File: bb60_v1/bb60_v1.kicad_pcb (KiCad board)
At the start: 2 copper layers, 145 parts, among them J1 Conn_01x04, SW1 SW_Push, SW2 SW_Push, U1 STM32F072CBTx, U2 XC6206PxxxMR, U3 USBLC6-2SC6

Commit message: rearranging pcb
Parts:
- moved C7 63.1 mm to (126.5, 175.0)
- moved C1 60.6 mm to (126.5, 171.5)
- moved C8 60.1 mm to (123.6, 175.0)
- moved C2 58.2 mm to (124.1, 171.5)
- moved C9 57.2 mm to (120.6, 175.0)
- moved C3 55.6 mm to (121.4, 171.5)
- moved C5 53.6 mm to (117.0, 171.5)
- moved C4 53.4 mm to (119.1, 171.5)
- moved C6 32.6 mm to (97.3, 172.6)
- moved R1 30.5 mm to (91.4, 172.0)
- moved R2 27.5 mm to (88.5, 172.0)
- moved R3 24.6 mm to (85.5, 172.0)
- moved U1 0.40 mm to (109.6, 174.4)
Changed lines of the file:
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@@
 	(footprint "Capacitor_SMD:C_0201_0603Metric"
 		(layer "B.Cu")
-		(at 63.448125 176.140625 180)
+		(at 120.598226 175.022022 180)
 		(descr "Capacitor SMD 0201 (0603 Metric), square (rectangular) end terminal, IPC-7351 nominal, (Body size source: https://www.vishay.com/docs/20052/crcw0201e3.pdf)")
 		(tags "capacitor")
@@
 	(footprint "Capacitor_SMD:C_0201_0603Metric"
 		(layer "B.Cu")
-		(at 65.898125 170.890625 180)
+		(at 126.456669 171.450144 180)
 		(descr "Capacitor SMD 0201 (0603 Metric), square (rectangular) end terminal, IPC-7351 nominal, (Body size source: https://www.vishay.com/docs/20052/crcw0201e3.pdf)")
 		(tags "capacitor")
@@
 	(footprint "Capacitor_SMD:C_0201_0603Metric"
 		(layer "B.Cu")
-		(at 63.448125 172.640625 180)
+		(at 126.456669 175.022022 180)
 		(descr "Capacitor SMD 0201 (0603 Metric), square (rectangular) end terminal, IPC-7351 nominal, (Body size source: https://www.vishay.com/docs/20052/crcw0201e3.pdf)")
 		(tags "capacitor")
@@
 	(footprint "Resistor_SMD:R_0201_0603Metric"
 		(layer "B.Cu")
-		(at 60.998125 170.890625 180)
+		(at 91.427889 172.045457 180)
 		(descr "Resistor SMD 0201 (0603 Metric), square (rectangular) end terminal, IPC-7351 nominal, (Body size source: https://www.vishay.com/docs/20052/crcw0201e3.pdf)")
 		(tags "resistor")
@@
 	(footprint "Capacitor_SMD:C_0201_0603Metric"
 		(layer "B.Cu")
-		(at 63.448125 170.890625 180)
+		(at 117.026348 171.450144 180)
 		(descr "Capacitor SMD 0201 (0603 Metric), square (rectangular) end terminal, IPC-7351 nominal, (Body size source: https://www.vishay.com/docs/20052/crcw0201e3.pdf)")
 		(tags "capacitor")
@@
 	(footprint "Resistor_SMD:R_0201_0603Metric"
 		(layer "B.Cu")
-		(at 60.998125 174.390625 180)
+		(at 85.474759 172.045457 180)
 		(descr "Resistor SMD 0201 (0603 Metric), square (rectangular) end terminal, IPC-7351 nominal, (Body size source: https://www.vishay.com/docs/20052/crcw0201e3.pdf)")
 		(tags "resistor")
@@
 	(footprint "Resistor_SMD:R_0201_0603Metric"
 		(layer "B.Cu")
-		(at 60.998125 172.640625 180)
+		(at 88.451324 172.045457 180)
 		(descr "Resistor SMD 0201 (0603 Metric), square (rectangular) end terminal, IPC-7351 nominal, (Body size source: https://www.vishay.com/docs/20052/crcw0201e3.pdf)")
 		(tags "resistor")
@@
 	(footprint "Package_QFP:LQFP-48_7x7mm_P0.5mm"
 		(layer "B.Cu")
-		(at 109.35875 174.11375 180)
+		(at 109.63766 174.400123 180)
 		(descr "LQFP, 48 Pin (JEDEC MS-026 variation BBC, 1.40mm body thickness, https://www.jedec.org/document_search?search_api_views_fulltext=MS-026, https://www.analog.com/media/en/package-pcb-resources/package/pkg_pdf/ltc-legacy-lqfp/05081760_a_lx48.pdf)")
 		(tags "LQFP QFP CASE-932AA CASE-932-03 C48-1 C48-2 C48-3 C48-5 C48-6 C48-6C PT0048A")
@@
 	(footprint "Capacitor_SMD:C_0201_0603Metric"
 		(layer "B.Cu")
-		(at 65.898125 172.640625 180)
+		(at 124.075417 171.450144 180)
 		(descr "Capacitor SMD 0201 (0603 Metric), square (rectangular) end terminal, IPC-7351 nominal, (Body size source: https://www.vishay.com/docs/20052/crcw0201e3.pdf)")
 		(tags "capacitor")
@@
 		)
 		(property "Value" "1N4148"
-			(at -35.82 -20.75 90)
+			(at -0.317673 -2.14298 90)
 			(layer "B.Fab")
 			(effects
@@
 	(footprint "Capacitor_SMD:C_0805_2012Metric"
 		(layer "B.Cu")
-		(at 65.481875 165.655625 180)
+		(at 97.276645 172.64077 180)
 		(descr "Capacitor SMD 0805 (2012 Metric), square (rectangular) end terminal, IPC-7351 nominal, (Body size source: IPC-SM-782 page 76, https://www.pcb-3d.com/wordpress/wp-content/uploads/ipc-sm-782a_amendment_1_and_2.pdf, https://docs.google.com/spreadsheets/d/1BsfQQcO9C6DZCsRaXUlFlo91Tg2WpOkGARC1WS5S8t0/edit?usp=sharing)")
 		(tags "capacitor")
@@
 	(footprint "Capacitor_SMD:C_0201_0603Metric"
 		(layer "B.Cu")
-		(at 65.898125 174.390625 180)
+		(at 121.443852 171.450144 180)
 		(descr "Capacitor SMD 0201 (0603 Metric), square (rectangular) end terminal, IPC-7351 nominal, (Body size source: https://www.vishay.com/docs/20052/crcw0201e3.pdf)")
 		(tags "capacitor")
@@
 	(footprint "Capacitor_SMD:C_0201_0603Metric"
 		(layer "B.Cu")
-		(at 65.898125 176.140625 180)
+		(at 119.0626 171.450144 180)
 		(descr "Capacitor SMD 0201 (0603 Metric), square (rectangular) end terminal, IPC-7351 nominal, (Body size source: https://www.vishay.com/docs/20052/crcw0201e3.pdf)")
 		(tags "capacitor")
@@
 	(footprint "Capacitor_SMD:C_0201_0603Metric"
 		(layer "B.Cu")
-		(at 63.448125 174.390625 180)
+		(at 123.574791 175.022022 180)
 		(descr "Capacitor SMD 0201 (0603 Metric), square (rectangular) end terminal, IPC-7351 nominal, (Body size source: https://www.vishay.com/docs/20052/crcw0201e3.pdf)")
 		(tags "capacitor")

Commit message: new traces made
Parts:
- moved D54 1.55 mm to (332.8, 205.7)
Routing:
- net /COL0: track 45.8 -> 115.0 mm, vias 0 -> 1
- net /COL12: track 62.3 -> 109.3 mm
- net /COL2: track 91.7 -> 125.7 mm, vias 0 -> 2
- net /COL1: track 85.1 -> 96.9 mm
- net Net-(D43-A): track 0.00 -> 7.17 mm
- net Net-(D41-A): track 0.00 -> 7.17 mm
- net Net-(D54-A): track 0.00 -> 7.12 mm

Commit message: minor changes
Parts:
- moved C1 66.0 mm to (60.6, 166.8)
- moved C2 66.0 mm to (58.2, 166.8)
- moved C3 66.0 mm to (55.6, 166.8)
- moved C4 66.0 mm to (53.2, 166.8)
- moved C5 66.0 mm to (51.2, 166.8)
- moved C6 66.0 mm to (31.4, 168.0)
- moved C7 66.0 mm to (60.6, 170.4)
- moved C8 66.0 mm to (57.7, 170.4)
- moved R2 66.0 mm to (22.6, 167.4)
- moved R3 66.0 mm to (19.6, 167.4)
- moved C9 66.0 mm to (54.8, 170.4)
- moved R1 66.0 mm to (25.6, 167.4)
- moved SW1 66.0 mm to (73.2, 170.1)
- moved SW2 66.0 mm to (67.3, 170.1)
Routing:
- net /ROW0: track 338.7 -> 257.2 mm
- net /ROW4: track 338.2 -> 260.6 mm
- net /ROW3: track 317.4 -> 254.6 mm
- net /ROW2: track 257.8 -> 221.5 mm, vias 2 -> 0
- net /COL2: track 125.7 -> 90.7 mm, vias 2 -> 0
- net /ROW1: track 261.8 -> 233.4 mm, vias 2 -> 0
- net /COL0: track 115.0 -> 91.5 mm, vias 1 -> 0
- net /COL1: track 96.9 -> 84.8 mm
- net /COL12: track 109.3 -> 106.0 mm
- net /COL6: track 95.1 -> 92.7 mm
- net /COL4: track 68.7 -> 67.7 mm
- net /COL11: track 88.0 -> 87.4 mm
- net /COL8: track 68.2 -> 67.7 mm

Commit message: added pcb outline to pcb
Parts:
- moved C6 127.3 mm to (43.3, 41.3)
- moved R1 127.3 mm to (37.4, 40.7)
- moved R2 127.3 mm to (34.4, 40.7)
- moved R3 127.3 mm to (31.5, 40.7)
- moved SW1 127.3 mm to (85.0, 43.3)
- moved SW2 127.3 mm to (79.1, 43.3)
- moved C1 127.3 mm to (72.4, 40.1)
- moved C2 127.3 mm to (70.1, 40.1)
- moved C3 127.3 mm to (67.4, 40.1)
- moved C4 127.3 mm to (65.0, 40.1)
- moved C5 127.3 mm to (63.0, 40.1)
- moved C7 127.3 mm to (72.4, 43.6)
- moved C8 127.3 mm to (69.6, 43.6)
- moved C9 127.3 mm to (66.6, 43.6)
- moved U2 67.5 mm to (100.0, 94.5)
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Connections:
- U1 pad 10: /COL6 -> /COL3
- U1 pad 11: /COL5 -> /COL2
- U1 pad 12: /COL4 -> /COL1
- U1 pad 13: /COL3 -> /COL6
- U1 pad 14: /COL2 -> /COL5
- U1 pad 16: /ROW2 -> /ROW4
- U1 pad 18: /ROW4 -> /ROW2
- U1 pad 43: /COL1 -> /COL4
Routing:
- net /COL3: track 67.7 -> 114.5 mm
- net /ROW1: track 233.4 -> 264.1 mm, vias 0 -> 2
- net GND: track 0.00 -> 30.4 mm
- net /COL2: track 90.7 -> 118.1 mm
- net /ROW2: track 221.5 -> 248.1 mm, vias 0 -> 2
- net +5V: track 0.00 -> 24.8 mm
- net /COL0: track 91.5 -> 108.0 mm, vias 0 -> 2
- net +3.3V: track 0.00 -> 10.3 mm, vias 0 -> 2
- net /COL1: track 84.8 -> 92.4 mm
- net /USB_D+: track 0.00 -> 5.38 mm
- net /USB_D-: track 0.00 -> 5.38 mm
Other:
- board outline added: 281 x 94.4 mm

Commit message: Routed traces columns 7-11
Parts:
- moved C1 111.0 mm to (182.7, 52.0)
- moved C4 111.0 mm to (175.3, 52.0)
- moved C7 111.0 mm to (182.7, 55.5)
- moved C8 111.0 mm to (179.9, 55.5)
- moved R3 111.0 mm to (141.8, 52.6)
- moved C2 111.0 mm to (180.4, 52.0)
- moved C3 111.0 mm to (177.7, 52.0)
- moved C5 111.0 mm to (173.3, 52.0)
- moved C6 111.0 mm to (153.6, 53.2)
- moved R1 111.0 mm to (147.7, 52.6)
- moved R2 111.0 mm to (144.7, 52.6)
- moved SW1 111.0 mm to (195.4, 55.2)
- moved SW2 111.0 mm to (189.4, 55.2)
- moved C9 111.0 mm to (176.9, 55.5)
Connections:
- U1 pad 2: /COL11 -> /COL7
- U1 pad 3: /COL10 -> /COL8
- U1 pad 5: /COL8 -> /COL10
- U1 pad 6: /COL7 -> /COL11
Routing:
- net /COL11: track 87.4 -> 281.9 mm, vias 0 -> 1
- net /COL10: track 67.7 -> 242.9 mm, vias 0 -> 1
- net /COL9: track 67.7 -> 223.7 mm, vias 0 -> 1
- net /COL8: track 67.7 -> 204.4 mm, vias 0 -> 1
- net /COL7: track 67.7 -> 185.1 mm, vias 0 -> 1
- net /ROW4: track 260.6 -> 316.7 mm, vias 0 -> 2
- net /ROW3: track 254.6 -> 283.5 mm
- net /ROW2: track 248.1 -> 260.9 mm

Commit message: minor changes
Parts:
- SW1, SW2: moved to F.Cu
- moved C1 128.3 mm to (63.7, 99.9)
- moved C4 128.3 mm to (56.3, 99.9)
- moved C7 128.3 mm to (63.7, 103.4)
- moved C8 128.3 mm to (60.8, 103.4)
- moved R3 128.3 mm to (22.7, 100.4)
- moved C2 128.3 mm to (61.3, 99.9)
- moved C3 128.3 mm to (58.7, 99.9)
- moved C5 128.3 mm to (54.3, 99.9)
- moved C6 128.3 mm to (34.5, 101.0)
- moved C9 128.3 mm to (57.8, 103.4)
- moved R1 128.3 mm to (28.7, 100.4)
- moved R2 128.3 mm to (25.7, 100.4)
- moved SW2 111.5 mm to (242.2, 153.5)
- moved SW1 105.1 mm to (232.7, 153.5)

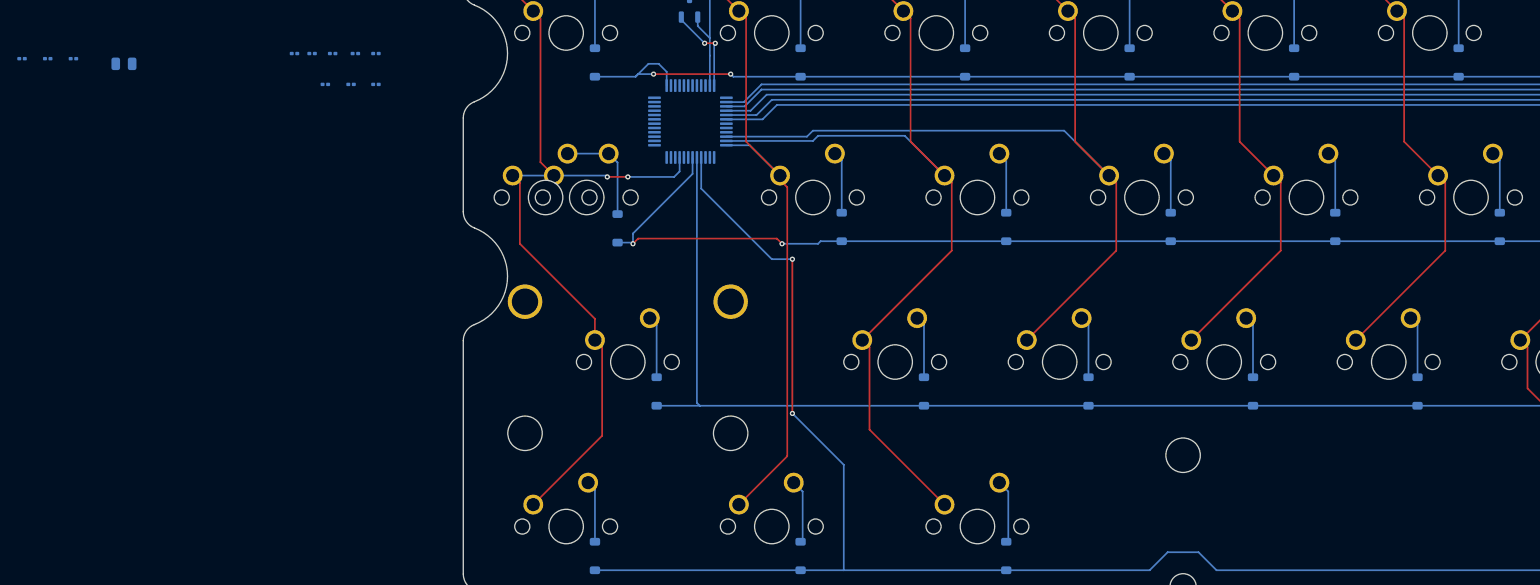
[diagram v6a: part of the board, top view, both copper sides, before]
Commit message: test export fab files
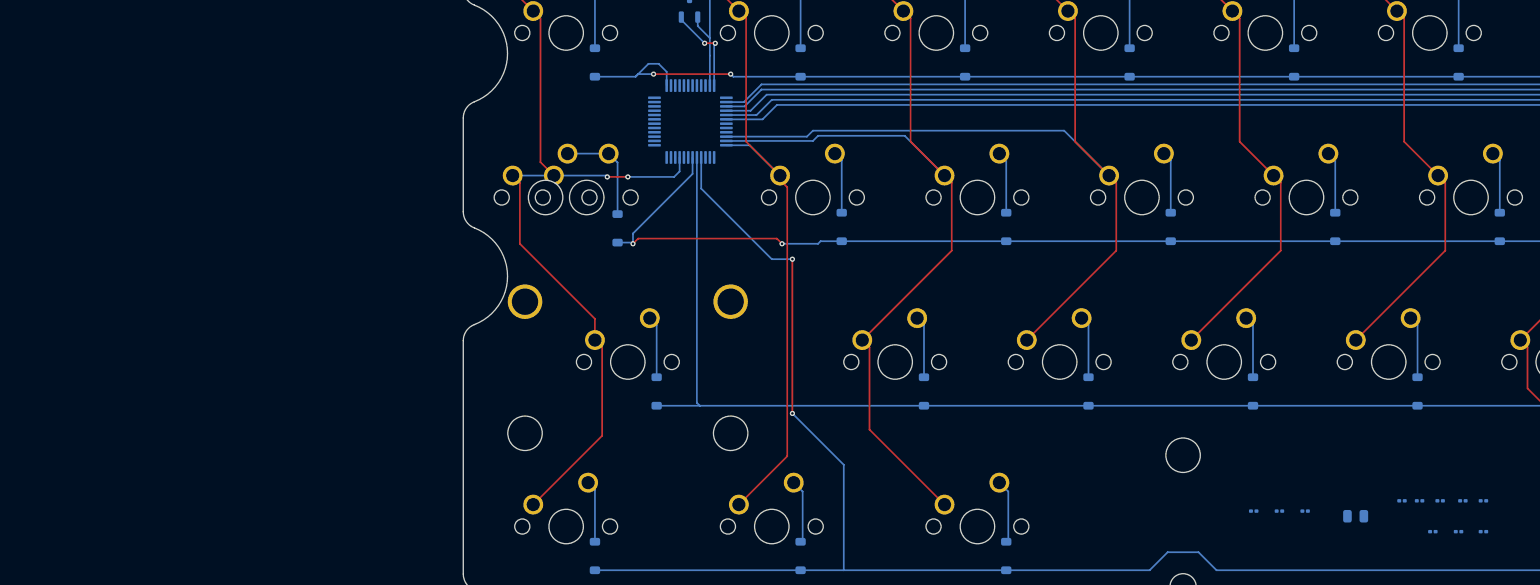
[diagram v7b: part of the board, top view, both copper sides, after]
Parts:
- moved R1 151.9 mm to (171.3, 152.8)
- moved R3 151.9 mm to (165.3, 152.8)
- moved C6 151.9 mm to (177.1, 153.4)
- moved R2 151.9 mm to (168.3, 152.8)
- moved C1 138.3 mm to (191.9, 151.6)
- moved C4 138.3 mm to (184.5, 151.6)
- moved C7 138.3 mm to (191.9, 155.2)
- moved C8 138.3 mm to (189.1, 155.2)
- moved C2 138.3 mm to (189.6, 151.6)
- moved C3 138.3 mm to (186.9, 151.6)
- moved C5 138.3 mm to (182.5, 151.6)
- moved C9 138.3 mm to (186.1, 155.2)
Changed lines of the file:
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@@
 	(footprint "Capacitor_SMD:C_0201_0603Metric"
 		(layer "B.Cu")
-		(at 57.83998 103.425518 180)
+		(at 186.082588 155.217749 180)
 		(descr "Capacitor SMD 0201 (0603 Metric), square (rectangular) end terminal, IPC-7351 nominal, (Body size source: https://www.vishay.com/docs/20052/crcw0201e3.pdf)")
 		(tags "capacitor")
@@
 	(footprint "Capacitor_SMD:C_0201_0603Metric"
 		(layer "B.Cu")
-		(at 63.698423 99.85364 180)
+		(at 191.941031 151.645871 180)
 		(descr "Capacitor SMD 0201 (0603 Metric), square (rectangular) end terminal, IPC-7351 nominal, (Body size source: https://www.vishay.com/docs/20052/crcw0201e3.pdf)")
 		(tags "capacitor")
@@
 	(footprint "Capacitor_SMD:C_0201_0603Metric"
 		(layer "B.Cu")
-		(at 63.698423 103.425518 180)
+		(at 191.941031 155.217749 180)
 		(descr "Capacitor SMD 0201 (0603 Metric), square (rectangular) end terminal, IPC-7351 nominal, (Body size source: https://www.vishay.com/docs/20052/crcw0201e3.pdf)")
 		(tags "capacitor")
@@
 	(footprint "Resistor_SMD:R_0201_0603Metric"
 		(layer "B.Cu")
-		(at 28.669643 100.448953 180)
+		(at 171.29445 152.836497 180)
 		(descr "Resistor SMD 0201 (0603 Metric), square (rectangular) end terminal, IPC-7351 nominal, (Body size source: https://www.vishay.com/docs/20052/crcw0201e3.pdf)")
 		(tags "resistor")
@@
 	(footprint "Capacitor_SMD:C_0201_0603Metric"
 		(layer "B.Cu")
-		(at 54.268102 99.85364 180)
+		(at 182.51071 151.645871 180)
 		(descr "Capacitor SMD 0201 (0603 Metric), square (rectangular) end terminal, IPC-7351 nominal, (Body size source: https://www.vishay.com/docs/20052/crcw0201e3.pdf)")
 		(tags "capacitor")
@@
 	(footprint "Resistor_SMD:R_0201_0603Metric"
 		(layer "B.Cu")
-		(at 22.716513 100.448953 180)
+		(at 165.34132 152.836497 180)
 		(descr "Resistor SMD 0201 (0603 Metric), square (rectangular) end terminal, IPC-7351 nominal, (Body size source: https://www.vishay.com/docs/20052/crcw0201e3.pdf)")
 		(tags "resistor")
@@
 	(footprint "Resistor_SMD:R_0201_0603Metric"
 		(layer "B.Cu")
-		(at 25.693078 100.448953 180)
+		(at 168.317885 152.836497 180)
 		(descr "Resistor SMD 0201 (0603 Metric), square (rectangular) end terminal, IPC-7351 nominal, (Body size source: https://www.vishay.com/docs/20052/crcw0201e3.pdf)")
 		(tags "resistor")
@@
 	(footprint "Capacitor_SMD:C_0201_0603Metric"
 		(layer "B.Cu")
-		(at 61.317171 99.85364 180)
+		(at 189.559779 151.645871 180)
 		(descr "Capacitor SMD 0201 (0603 Metric), square (rectangular) end terminal, IPC-7351 nominal, (Body size source: https://www.vishay.com/docs/20052/crcw0201e3.pdf)")
 		(tags "capacitor")
@@
 	(footprint "Capacitor_SMD:C_0805_2012Metric"
 		(layer "B.Cu")
-		(at 34.518399 101.044266 180)
+		(at 177.143206 153.43181 180)
 		(descr "Capacitor SMD 0805 (2012 Metric), square (rectangular) end terminal, IPC-7351 nominal, (Body size source: IPC-SM-782 page 76, https://www.pcb-3d.com/wordpress/wp-content/uploads/ipc-sm-782a_amendment_1_and_2.pdf, https://docs.google.com/spreadsheets/d/1BsfQQcO9C6DZCsRaXUlFlo91Tg2WpOkGARC1WS5S8t0/edit?usp=sharing)")
 		(tags "capacitor")
@@
 	(footprint "Capacitor_SMD:C_0201_0603Metric"
 		(layer "B.Cu")
-		(at 58.685606 99.85364 180)
+		(at 186.928214 151.645871 180)
 		(descr "Capacitor SMD 0201 (0603 Metric), square (rectangular) end terminal, IPC-7351 nominal, (Body size source: https://www.vishay.com/docs/20052/crcw0201e3.pdf)")
 		(tags "capacitor")
@@
 	(footprint "Capacitor_SMD:C_0201_0603Metric"
 		(layer "B.Cu")
-		(at 56.304354 99.85364 180)
+		(at 184.546962 151.645871 180)
 		(descr "Capacitor SMD 0201 (0603 Metric), square (rectangular) end terminal, IPC-7351 nominal, (Body size source: https://www.vishay.com/docs/20052/crcw0201e3.pdf)")
 		(tags "capacitor")
@@
 	(footprint "Capacitor_SMD:C_0201_0603Metric"
 		(layer "B.Cu")
-		(at 60.816545 103.425518 180)
+		(at 189.059153 155.217749 180)
 		(descr "Capacitor SMD 0201 (0603 Metric), square (rectangular) end terminal, IPC-7351 nominal, (Body size source: https://www.vishay.com/docs/20052/crcw0201e3.pdf)")
 		(tags "capacitor")
